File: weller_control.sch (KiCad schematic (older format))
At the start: 19 parts, among them J2 AudioJack3_Ground_SwitchTR, Q1 DMP2018LFK, U2 LTC4440ES6, U3 MCP603-xCH

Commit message: duży update, gotowe pcb
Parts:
- C11: footprint (none) -> Capacitor_SMD:C_0603_1608Metric
- R7: footprint Resistor_SMD:R_0402_1005Metric -> Resistor_SMD:R_0603_1608Metric
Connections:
- wire segments 51 -> 53
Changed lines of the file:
@@
 EESchema Schematic File Version 4
+LIBS:WELLER-cache
 EELAYER 29 0
 EELAYER END
@@
 F 0 "R7" V 3793 3050 50  0000 C CNN
 F 1 "100" V 3884 3050 50  0000 C CNN
-F 2 "Resistor_SMD:R_0402_1005Metric" V 3930 3050 50  0001 C CNN
+F 2 "Resistor_SMD:R_0603_1608Metric" V 3930 3050 50  0001 C CNN
 F 3 "~" H 4000 3050 50  0001 C CNN
 	1    4000 3050
@@
 Connection ~ 5750 6000
 Wire Wire Line
-	5750 6000 5750 6250
+	5750 6000 5750 6150
 Wire Wire Line
 	5750 5700 5750 6000
@@
 	1    0    0    -1
 $EndComp
-NoConn ~ 5750 5000
 Text Notes 7200 4700 0    50   ~ 0
 sprawdzenie czy na przypisanie pinów na footptincie piny się zgadza\n
@@
 F 0 "C11" H 6665 5496 50  0000 L CNN
 F 1 "n.c." H 6665 5405 50  0000 L CNN
-F 2 "" H 6588 5300 50  0001 C CNN
+F 2 "Capacitor_SMD:C_0603_1608Metric" H 6588 5300 50  0001 C CNN
 F 3 "~" H 6550 5450 50  0001 C CNN
 	1    6550 5450
@@
 Wire Wire Line
 	6600 2600 6650 2600
+Text HLabel 5750 4950 1    50   Input ~ 0
+3.3V_analog
+Wire Wire Line
+	5750 4950 5750 5000
+NoConn ~ 7150 3600
+$Comp
+L power:PWR_FLAG #FLG0104
+U 1 1 5CF26DBB
+P 5750 6150
+F 0 "#FLG0104" H 5750 6225 50  0001 C CNN
+F 1 "PWR_FLAG" V 5750 6278 50  0000 L CNN
+F 2 "" H 5750 6150 50  0001 C CNN
+F 3 "~" H 5750 6150 50  0001 C CNN
+	1    5750 6150
+	0    1    1    0
+$EndComp
+Connection ~ 5750 6150
+Wire Wire Line
+	5750 6150 5750 6250
 $EndSCHEMATC

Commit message: poprawki na sch
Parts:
- removed J2: AudioJack3_Ground_SwitchTR, Connector_Audio:Jack_3.5mm_CUI_SJ-3524-SMT_Horizontal, symbol Connector:AudioJack3_SwitchTR
- added J2: AudioJack2_Ground_SwitchT, Connector_Audio:Jack_3.5mm_CUI_SJ-3524-SMT_Horizontal, symbol Connector:AudioJack2_Ground_SwitchT
- U3: footprint Package_TO_SOT_SMD:SOT-23-5_HandSoldering -> TO_SOT_Packages_SMD:SOT-23-6
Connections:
- wire segments 53 -> 52
- no-connect marks 1 -> 0
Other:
- note added: "from tip: ground, sensor, heater"
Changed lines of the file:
@@
 EESchema Schematic File Version 4
 LIBS:WELLER-cache
-EELAYER 29 0
+EELAYER 26 0
 EELAYER END
 $Descr A4 11693 8268
@@
 L power:GND #PWR?
 U 1 1 5CBA0B9E
-P 7050 3950
+P 7350 3950
 AR Path="/5CB5C0EA/5CBA0B9E" Ref="#PWR?"  Part="1"
 AR Path="/5CB9B8FA/5CBA0B9E" Ref="#PWR0115"  Part="1"
-F 0 "#PWR0115" H 7050 3700 50  0001 C CNN
-F 1 "GND" H 7055 3777 50  0000 C CNN
-F 2 "" H 7050 3950 50  0001 C CNN
-F 3 "" H 7050 3950 50  0001 C CNN
-	1    7050 3950
-	1    0    0    -1
-$EndComp
-Wire Wire Line
-	7150 3800 7050 3800
-Wire Wire Line
-	7050 3800 7050 3950
-Wire Wire Line
-	7150 3700 7000 3700
-Text Label 7000 3700 2    50   ~ 0
-termocouple+
-Text Label 7050 3500 2    50   ~ 0
+F 0 "#PWR0115" H 7350 3700 50  0001 C CNN
+F 1 "GND" H 7355 3777 50  0000 C CNN
+F 2 "" H 7350 3950 50  0001 C CNN
+F 3 "" H 7350 3950 50  0001 C CNN
+	1    7350 3950
+	1    0    0    -1
+$EndComp
+Text Label 7050 3600 2    50   ~ 0
 heater
 Text HLabel 6300 2550 1    50   Input ~ 0
@@
 F 0 "U3" H 6194 5346 50  0000 L CNN
 F 1 "MCP603-xCH" H 6194 5255 50  0000 L CNN
-F 2 "Package_TO_SOT_SMD:SOT-23-5_HandSoldering" H 5850 5300 50  0001 L CNN
+F 2 "TO_SOT_Packages_SMD:SOT-23-6" H 5850 5300 50  0001 L CNN
 F 3 "https://www.tme.eu/Document/718e1e465ad4ed1ffbd9a510b0eda58e/mcp6031.pdf" H 5900 5500 50  0001 C CNN
 	1    5850 5300
 	1    0    0    -1
 $EndComp
-Text Notes 7200 4700 0    50   ~ 0
+Text Notes 7250 3150 0    50   ~ 0
 sprawdzenie czy na przypisanie pinów na footptincie piny się zgadza\n
 Text Label 4000 5200 2    50   ~ 0
@@
 Wire Wire Line
 	7250 5300 7050 5300
-Wire Wire Line
-	6900 3400 7150 3400
-Text HLabel 6900 3400 1    50   BiDi ~ 0
+Text HLabel 7000 3700 0    50   BiDi ~ 0
 weller_connected_pin
 Wire Wire Line
@@
 Wire Wire Line
 	5300 3500 6300 3500
-$Comp
-L Connector:AudioJack3_SwitchTR J2
-U 1 1 5CBFD79A
-P 7350 3700
-F 0 "J2" H 7070 3476 50  0000 R CNN
-F 1 "AudioJack3_Ground_SwitchTR" H 7070 3567 50  0000 R CNN
-F 2 "Connector_Audio:Jack_3.5mm_CUI_SJ-3524-SMT_Horizontal" H 7350 3700 50  0001 C CNN
-F 3 "~" H 7350 3700 50  0001 C CNN
-	1    7350 3700
-	-1   0    0    1
-$EndComp
 $Comp
 L Device:C C19
@@
 Wire Wire Line
 	5750 4950 5750 5000
-NoConn ~ 7150 3600
 $Comp
 L power:PWR_FLAG #FLG0104
@@
 Wire Wire Line
 	5750 6150 5750 6250
+$Comp
+L Connector:AudioJack2_Ground_SwitchT J2
+U 1 1 5CEFB0EB
+P 7350 3600
+F 0 "J2" H 7170 3570 50  0000 R CNN
+F 1 "AudioJack2_Ground_SwitchT" H 7170 3479 50  0000 R CNN
+F 2 "Connector_Audio:Jack_3.5mm_CUI_SJ-3524-SMT_Horizontal" H 7350 3600 50  0001 C CNN
+F 3 "~" H 7350 3600 50  0001 C CNN
+	1    7350 3600
+	-1   0    0    -1
+$EndComp
+Text Label 7100 3500 2    50   ~ 0
+termocouple+
+Wire Wire Line
+	7350 3900 7350 3950
+Wire Wire Line
+	7150 3700 7000 3700
+Wire Wire Line
+	7050 3600 7150 3600
+Text Notes 7250 3300 0    50   ~ 0
+from tip: ground, sensor, heater
 $EndSCHEMATC

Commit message: duży update, drc przechodzi
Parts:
- removed J2: AudioJack2_Ground_SwitchT, Connector_Audio:Jack_3.5mm_CUI_SJ-3524-SMT_Horizontal, symbol Connector:AudioJack2_Ground_SwitchT
- added J2: AudioJack3_Ground_SwitchR, symbols:Jack Audio 1503 20, symbol Connector:AudioJack3_Ground_SwitchR
- R7: footprint Resistor_SMD:R_0603_1608Metric -> Resistor_SMD:R_1206_3216Metric
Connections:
- wire segments 52 -> 54
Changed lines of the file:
@@
 EESchema Schematic File Version 4
 LIBS:WELLER-cache
-EELAYER 26 0
+EELAYER 29 0
 EELAYER END
 $Descr A4 11693 8268
@@
 Comment4 ""
 $EndDescr
-$Comp
-L power:GND #PWR?
-U 1 1 5CBA0B9E
-P 7350 3950
-AR Path="/5CB5C0EA/5CBA0B9E" Ref="#PWR?"  Part="1"
-AR Path="/5CB9B8FA/5CBA0B9E" Ref="#PWR0115"  Part="1"
-F 0 "#PWR0115" H 7350 3700 50  0001 C CNN
-F 1 "GND" H 7355 3777 50  0000 C CNN
-F 2 "" H 7350 3950 50  0001 C CNN
-F 3 "" H 7350 3950 50  0001 C CNN
-	1    7350 3950
-	1    0    0    -1
-$EndComp
-Text Label 7050 3600 2    50   ~ 0
-heater
 Text HLabel 6300 2550 1    50   Input ~ 0
 12V
@@
 F 0 "R7" V 3793 3050 50  0000 C CNN
 F 1 "100" V 3884 3050 50  0000 C CNN
-F 2 "Resistor_SMD:R_0603_1608Metric" V 3930 3050 50  0001 C CNN
+F 2 "Resistor_SMD:R_1206_3216Metric" V 3930 3050 50  0001 C CNN
 F 3 "~" H 4000 3050 50  0001 C CNN
 	1    4000 3050
@@
 	5200 2850 5100 2850
 Connection ~ 5100 2850
-Connection ~ 6300 3500
-Wire Wire Line
-	6300 3500 7150 3500
 Text HLabel 3550 3050 0    50   Input ~ 0
 HeaterDrivePWM
-$Comp
-L Transistor_FET:DMP3013SFV Q1
-U 1 1 5CBB49B6
-P 6200 3050
-F 0 "Q1" H 6406 3096 50  0000 L CNN
-F 1 "DMP2018LFK" H 6406 3005 50  0000 L CNN
-F 2 "Package_SON:Diodes_PowerDI3333-8" H 6400 2975 50  0001 L CIN
-F 3 "https://www.diodes.com/assets/Datasheets/DMP3013SFV.pdf" V 6200 3050 50  0001 L CNN
-	1    6200 3050
-	1    0    0    -1
-$EndComp
 Wire Wire Line
 	5100 3050 6000 3050
@@
 Connection ~ 5750 6000
 Wire Wire Line
-	5750 6000 5750 6150
-Wire Wire Line
 	5750 5700 5750 6000
 Wire Wire Line
@@
 	1    0    0    -1
 $EndComp
-Text Notes 7250 3150 0    50   ~ 0
+Text Notes 7100 2800 0    50   ~ 0
 sprawdzenie czy na przypisanie pinów na footptincie piny się zgadza\n
 Text Label 4000 5200 2    50   ~ 0
@@
 Wire Wire Line
 	7250 5300 7050 5300
-Text HLabel 7000 3700 0    50   BiDi ~ 0
+Text HLabel 7450 3400 0    50   BiDi ~ 0
 weller_connected_pin
 Wire Wire Line
@@
 Wire Wire Line
 	5750 4950 5750 5000
-$Comp
-L power:PWR_FLAG #FLG0104
-U 1 1 5CF26DBB
-P 5750 6150
-F 0 "#FLG0104" H 5750 6225 50  0001 C CNN
-F 1 "PWR_FLAG" V 5750 6278 50  0000 L CNN
-F 2 "" H 5750 6150 50  0001 C CNN
-F 3 "~" H 5750 6150 50  0001 C CNN
-	1    5750 6150
-	0    1    1    0
-$EndComp
-Connection ~ 5750 6150
-Wire Wire Line
-	5750 6150 5750 6250
-$Comp
-L Connector:AudioJack2_Ground_SwitchT J2
-U 1 1 5CEFB0EB
-P 7350 3600
-F 0 "J2" H 7170 3570 50  0000 R CNN
-F 1 "AudioJack2_Ground_SwitchT" H 7170 3479 50  0000 R CNN
-F 2 "Connector_Audio:Jack_3.5mm_CUI_SJ-3524-SMT_Horizontal" H 7350 3600 50  0001 C CNN
-F 3 "~" H 7350 3600 50  0001 C CNN
-	1    7350 3600
+Text Label 7550 3200 2    50   ~ 0
+termocouple+
+Wire Wire Line
+	7600 3400 7450 3400
+Text Notes 7100 2950 0    50   ~ 0
+from tip: ground, sensor, heater
+$Comp
+L Transistor_FET:DMP3013SFV Q1
+U 1 1 5CBB49B6
+P 6200 3050
+F 0 "Q1" H 6406 3096 50  0000 L CNN
+F 1 "DMP2018LFK" H 6406 3005 50  0000 L CNN
+F 2 "Package_SON:Diodes_PowerDI3333-8" H 6400 2975 50  0001 L CIN
+F 3 "https://www.diodes.com/assets/Datasheets/DMP3013SFV.pdf" V 6200 3050 50  0001 L CNN
+	1    6200 3050
+	1    0    0    -1
+$EndComp
+$Comp
+L power:GND #PWR?
+U 1 1 5CBA0B9E
+P 7800 3850
+AR Path="/5CB5C0EA/5CBA0B9E" Ref="#PWR?"  Part="1"
+AR Path="/5CB9B8FA/5CBA0B9E" Ref="#PWR0115"  Part="1"
+F 0 "#PWR0115" H 7800 3600 50  0001 C CNN
+F 1 "GND" H 7805 3677 50  0000 C CNN
+F 2 "" H 7800 3850 50  0001 C CNN
+F 3 "" H 7800 3850 50  0001 C CNN
+	1    7800 3850
+	1    0    0    -1
+$EndComp
+Wire Wire Line
+	7800 3800 7800 3850
+$Comp
+L Connector:AudioJack3_Ground_SwitchR J2
+U 1 1 5CFC3271
+P 7800 3300
+F 0 "J2" H 7520 3168 50  0000 R CNN
+F 1 "AudioJack3_Ground_SwitchR" H 7520 3077 50  0000 R CNN
+F 2 "symbols:Jack Audio 1503 20" H 7800 3300 50  0001 C CNN
+F 3 "~" H 7800 3300 50  0001 C CNN
+	1    7800 3300
 	-1   0    0    -1
 $EndComp
 Text Label 7100 3500 2    50   ~ 0
-termocouple+
-Wire Wire Line
-	7350 3900 7350 3950
-Wire Wire Line
-	7150 3700 7000 3700
-Wire Wire Line
-	7050 3600 7150 3600
-Text Notes 7250 3300 0    50   ~ 0
-from tip: ground, sensor, heater
+heater
+Wire Wire Line
+	7550 3200 7600 3200
+Wire Wire Line
+	6300 3500 7200 3500
+Connection ~ 6300 3500
+Wire Wire Line
+	7600 3300 7200 3300
+Wire Wire Line
+	7200 3300 7200 3500
+Connection ~ 7200 3500
+Wire Wire Line
+	7200 3500 7600 3500
+Wire Wire Line
+	5750 6000 5750 6250
 $EndSCHEMATC

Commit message: poprawki głownie na pcb zaokrąglenie strony z grotem
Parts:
- removed D6: 1n4148, Diode_SMD:D_0805_2012Metric, symbol Device:D
- removed U2: LTC4440ES6, Package_TO_SOT_SMD:SOT-23-6, symbol Driver_FET:LTC4440ES6
- added C26: 100n, Capacitor_SMD:C_0603_1608Metric_Pad1.05x0.95mm_HandSolder, symbol Device:C
- added D6: 1N4148, Diode_SMD:D_0805_2012Metric, symbol Diode:1N4148
- added U2: LTC4440IS6, Package_TO_SOT_SMD:SOT-23-6, symbol Driver_FET:LTC4440IS6
- C8: value 100n -> 10uF; footprint Capacitor_SMD:C_0603_1608Metric_Pad1.05x0.95mm_HandSolder -> Capacitor_SMD:C_0805_2012Metric
- Q1: Pole4 (none) -> ${KISYS3DMOD}/Package_DFN_QFN.3dshapes/DFN-8-1EP_3x3mm_P0.6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
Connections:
- wire segments 54 -> 57
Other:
- moved on the sheet: C8, R7
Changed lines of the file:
@@
 	6300 2550 6300 2600
 Wire Wire Line
-	6300 3250 6300 3500
-$Comp
-L Driver_FET:LTC4440ES6 U2
-U 1 1 5CBAC998
-P 4700 3050
-F 0 "U2" H 4700 3631 50  0000 C CNN
-F 1 "LTC4440ES6" H 4700 3540 50  0000 C CNN
-F 2 "Package_TO_SOT_SMD:SOT-23-6" H 4700 2650 50  0001 C CNN
-F 3 "https://www.analog.com/media/en/technical-documentation/data-sheets/4440fb.pdf" H 4600 3500 50  0001 C CNN
-	1    4700 3050
-	1    0    0    -1
-$EndComp
-Text HLabel 4600 2200 1    50   Input ~ 0
+	6300 3250 6300 3300
+Text HLabel 4550 2150 1    50   Input ~ 0
 12V
 Wire Wire Line
-	4600 2200 4600 2400
+	4550 2150 4550 2350
 $Comp
 L power:GND #PWR?
 U 1 1 5CBAEA63
-P 4700 3850
+P 4650 3650
 AR Path="/5CB5C0EA/5CBAEA63" Ref="#PWR?"  Part="1"
 AR Path="/5CB9B8FA/5CBAEA63" Ref="#PWR0116"  Part="1"
-F 0 "#PWR0116" H 4700 3600 50  0001 C CNN
-F 1 "GND" H 4705 3677 50  0000 C CNN
-F 2 "" H 4700 3850 50  0001 C CNN
-F 3 "" H 4700 3850 50  0001 C CNN
-	1    4700 3850
-	1    0    0    -1
-$EndComp
-Wire Wire Line
-	4700 3850 4700 3350
+F 0 "#PWR0116" H 4650 3400 50  0001 C CNN
+F 1 "GND" H 4655 3477 50  0000 C CNN
+F 2 "" H 4650 3650 50  0001 C CNN
+F 3 "" H 4650 3650 50  0001 C CNN
+	1    4650 3650
+	1    0    0    -1
+$EndComp
+Wire Wire Line
+	4650 3650 4650 3350
 $Comp
 L Device:R R7
 U 1 1 5CBB027F
-P 4000 3050
-F 0 "R7" V 3793 3050 50  0000 C CNN
-F 1 "100" V 3884 3050 50  0000 C CNN
-F 2 "Resistor_SMD:R_1206_3216Metric" V 3930 3050 50  0001 C CNN
-F 3 "~" H 4000 3050 50  0001 C CNN
-	1    4000 3050
+P 3800 3050
+F 0 "R7" V 3593 3050 50  0000 C CNN
+F 1 "100" V 3684 3050 50  0000 C CNN
+F 2 "Resistor_SMD:R_1206_3216Metric" V 3730 3050 50  0001 C CNN
+F 3 "~" H 3800 3050 50  0001 C CNN
+	1    3800 3050
 	0    1    1    0
 $EndComp
 Wire Wire Line
-	5100 3150 5200 3150
-Wire Wire Line
-	5300 3150 5300 3500
-$Comp
-L Device:D D6
-U 1 1 5CBB1370
-P 4900 2400
-F 0 "D6" H 4900 2184 50  0000 C CNN
-F 1 "1n4148" H 4900 2275 50  0000 C CNN
-F 2 "Diode_SMD:D_0805_2012Metric" H 4900 2400 50  0001 C CNN
-F 3 "~" H 4900 2400 50  0001 C CNN
-	1    4900 2400
-	-1   0    0    1
-$EndComp
-Wire Wire Line
-	4750 2400 4600 2400
-Connection ~ 4600 2400
-Wire Wire Line
-	4600 2400 4600 2650
-Wire Wire Line
-	5050 2400 5100 2400
-Wire Wire Line
-	5100 2400 5100 2850
-$Comp
-L Device:C C7
-U 1 1 5CBB2260
-P 5200 3000
-F 0 "C7" H 5315 3046 50  0000 L CNN
-F 1 "100n" H 5315 2955 50  0000 L CNN
-F 2 "Capacitor_SMD:C_0603_1608Metric_Pad1.05x0.95mm_HandSolder" H 5238 2850 50  0001 C CNN
-F 3 "~" H 5200 3000 50  0001 C CNN
-	1    5200 3000
-	1    0    0    -1
-$EndComp
-Connection ~ 5200 3150
-Wire Wire Line
-	5200 3150 5300 3150
-Wire Wire Line
-	5200 2850 5100 2850
-Connection ~ 5100 2850
-Text HLabel 3550 3050 0    50   Input ~ 0
+	4700 2350 4550 2350
+Connection ~ 4550 2350
+Text HLabel 3350 3050 0    50   Input ~ 0
 HeaterDrivePWM
 Wire Wire Line
-	5100 3050 6000 3050
-Wire Wire Line
-	3550 3050 3850 3050
-Wire Wire Line
-	4150 3050 4300 3050
+	3350 3050 3650 3050
 $Comp
 L Device:R R12
@@
 Text HLabel 7450 3400 0    50   BiDi ~ 0
 weller_connected_pin
-Wire Wire Line
-	5300 3850 5300 3800
-$Comp
-L power:GND #PWR?
-U 1 1 5CBA9A21
-P 5300 3850
-AR Path="/5CB5C0EA/5CBA9A21" Ref="#PWR?"  Part="1"
-AR Path="/5CB9B8FA/5CBA9A21" Ref="#PWR0122"  Part="1"
-F 0 "#PWR0122" H 5300 3600 50  0001 C CNN
-F 1 "GND" H 5305 3677 50  0000 C CNN
-F 2 "" H 5300 3850 50  0001 C CNN
-F 3 "" H 5300 3850 50  0001 C CNN
-	1    5300 3850
-	1    0    0    -1
-$EndComp
 $Comp
 L Device:C C8
 U 1 1 5CBA90B4
-P 5300 3650
-F 0 "C8" H 5415 3696 50  0000 L CNN
-F 1 "100n" H 5415 3605 50  0000 L CNN
-F 2 "Capacitor_SMD:C_0603_1608Metric_Pad1.05x0.95mm_HandSolder" H 5338 3500 50  0001 C CNN
-F 3 "~" H 5300 3650 50  0001 C CNN
-	1    5300 3650
-	1    0    0    -1
-$EndComp
-Connection ~ 5300 3500
-Wire Wire Line
-	5300 3500 6300 3500
+P 4850 2350
+F 0 "C8" H 4965 2396 50  0000 L CNN
+F 1 "10uF" H 4965 2305 50  0000 L CNN
+F 2 "Capacitor_SMD:C_0805_2012Metric" H 4888 2200 50  0001 C CNN
+F 3 "~" H 4850 2350 50  0001 C CNN
+	1    4850 2350
+	0    1    -1   0
+$EndComp
 $Comp
 L Device:C C19
@@
 F 2 "Package_SON:Diodes_PowerDI3333-8" H 6400 2975 50  0001 L CIN
 F 3 "https://www.diodes.com/assets/Datasheets/DMP3013SFV.pdf" V 6200 3050 50  0001 L CNN
+F 4 "${KISYS3DMOD}/Package_DFN_QFN.3dshapes/DFN-8-1EP_3x3mm_P0.65mm_EP1.55x2.4mm.wrl" H 6200 3050 50  0001 C CNN "Pole4"
 	1    6200 3050
-	1    0    0    -1
+	1    0    0    1
 $EndComp
 $Comp
@@
 Wire Wire Line
 	6300 3500 7200 3500
-Connection ~ 6300 3500
 Wire Wire Line
 	7600 3300 7200 3300
@@
 Wire Wire Line
 	5750 6000 5750 6250
+$Comp
+L Device:C C7
+U 1 1 5D187BE9
+P 4400 2350
+F 0 "C7" H 4515 2396 50  0000 L CNN
+F 1 "100n" H 4515 2305 50  0000 L CNN
+F 2 "Capacitor_SMD:C_0603_1608Metric_Pad1.05x0.95mm_HandSolder" H 4438 2200 50  0001 C CNN
+F 3 "~" H 4400 2350 50  0001 C CNN
+	1    4400 2350
+	0    1    -1   0
+$EndComp
+$Comp
+L power:GND #PWR?
+U 1 1 5D18AED0
+P 4150 2350
+AR Path="/5CB5C0EA/5D18AED0" Ref="#PWR?"  Part="1"
+AR Path="/5CB9B8FA/5D18AED0" Ref="#PWR0122"  Part="1"
+F 0 "#PWR0122" H 4150 2100 50  0001 C CNN
+F 1 "GND" H 4155 2177 50  0000 C CNN
+F 2 "" H 4150 2350 50  0001 C CNN
+F 3 "" H 4150 2350 50  0001 C CNN
+	1    4150 2350
+	0    1    1    0
+$EndComp
+Wire Wire Line
+	4150 2350 4250 2350
+$Comp
+L Driver_FET:LTC4440IS6 U2
+U 1 1 5D1044C6
+P 4650 3050
+F 0 "U2" H 4100 3550 50  0000 C CNN
+F 1 "LTC4440IS6" H 4250 3450 50  0000 C CNN
+F 2 "Package_TO_SOT_SMD:SOT-23-6" H 4650 2650 50  0001 C CNN
+F 3 "https://www.analog.com/media/en/technical-documentation/data-sheets/4440fb.pdf" H 4550 3500 50  0001 C CNN
+	1    4650 3050
+	1    0    0    -1
+$EndComp
+$Comp
+L Diode:1N4148 D6
+U 1 1 5D104CD3
+P 4950 2650
+F 0 "D6" H 4950 2434 50  0000 C CNN
+F 1 "1N4148" H 4950 2525 50  0000 C CNN
+F 2 "Diode_SMD:D_0805_2012Metric" H 4950 2475 50  0001 C CNN
+F 3 "https://assets.nexperia.com/documents/data-sheet/1N4148_1N4448.pdf" H 4950 2650 50  0001 C CNN
+	1    4950 2650
+	-1   0    0    1
+$EndComp
+Wire Wire Line
+	3950 3050 4250 3050
+Wire Wire Line
+	4550 2350 4550 2650
+$Comp
+L power:GND #PWR?
+U 1 1 5D10E4EA
+P 5100 2350
+AR Path="/5CB5C0EA/5D10E4EA" Ref="#PWR?"  Part="1"
+AR Path="/5CB9B8FA/5D10E4EA" Ref="#PWR0143"  Part="1"
+F 0 "#PWR0143" H 5100 2100 50  0001 C CNN
+F 1 "GND" H 5105 2177 50  0000 C CNN
+F 2 "" H 5100 2350 50  0001 C CNN
+F 3 "" H 5100 2350 50  0001 C CNN
+	1    5100 2350
+	0    -1   -1   0
+$EndComp
+Wire Wire Line
+	5000 2350 5100 2350
+Wire Wire Line
+	5050 3150 5150 3150
+Wire Wire Line
+	5850 3150 5850 3300
+Wire Wire Line
+	5850 3300 6300 3300
+Connection ~ 6300 3300
+Wire Wire Line
+	6300 3300 6300 3500
+Wire Wire Line
+	5050 3050 6000 3050
+Wire Wire Line
+	4550 2650 4800 2650
+Connection ~ 4550 2650
+Wire Wire Line
+	5150 2650 5100 2650
+Wire Wire Line
+	5050 2850 5150 2850
+Wire Wire Line
+	5150 2850 5150 2650
+$Comp
+L Device:C C26
+U 1 1 5D1181DD
+P 5150 3000
+F 0 "C26" H 5265 3046 50  0000 L CNN
+F 1 "100n" H 5265 2955 50  0000 L CNN
+F 2 "Capacitor_SMD:C_0603_1608Metric_Pad1.05x0.95mm_HandSolder" H 5188 2850 50  0001 C CNN
+F 3 "~" H 5150 3000 50  0001 C CNN
+	1    5150 3000
+	1    0    0    1
+$EndComp
+Connection ~ 5150 3150
+Wire Wire Line
+	5150 3150 5850 3150
+Connection ~ 5150 2850
 $EndSCHEMATC

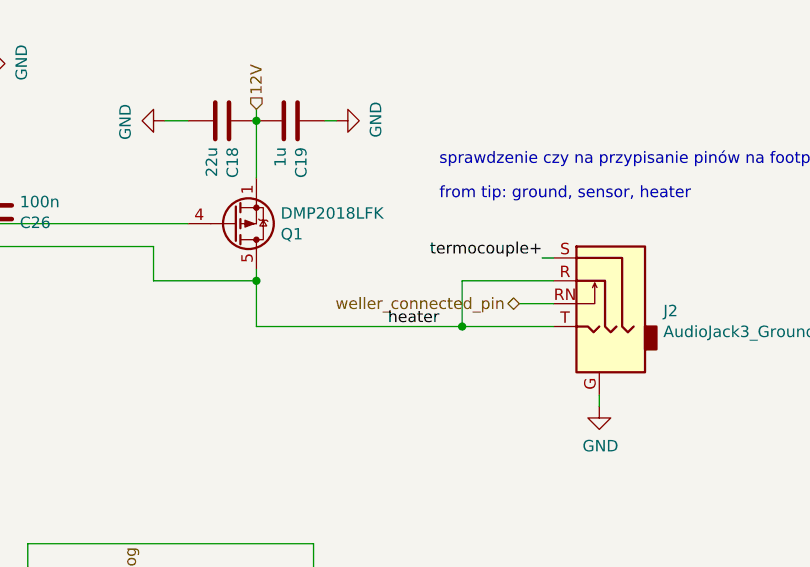
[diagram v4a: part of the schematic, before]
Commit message: wyciecie przy gnieździe jack - dodanie 3d gniazda, update jpg
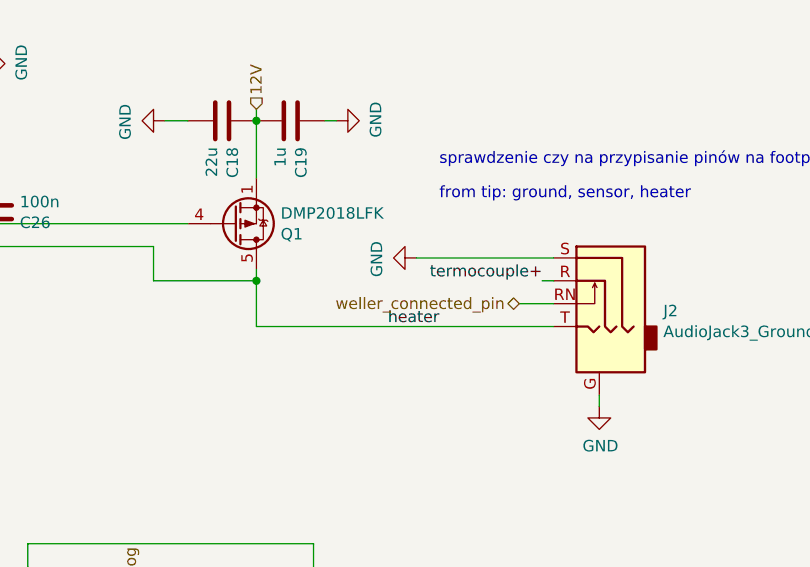
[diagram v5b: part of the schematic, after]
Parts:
- J2: footprint symbols:Jack Audio 1503 20 -> symbols:Jack Audio150320cutout
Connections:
- net GND: now also J2.S
- net heater: no longer J2.R
- net termocouple+: now also J2.R; no longer J2.S
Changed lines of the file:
@@
 Wire Wire Line
 	5750 4950 5750 5000
-Text Label 7550 3200 2    50   ~ 0
+Text Label 7550 3300 2    50   ~ 0
 termocouple+
 Wire Wire Line
@@
 F 0 "J2" H 7520 3168 50  0000 R CNN
 F 1 "AudioJack3_Ground_SwitchR" H 7520 3077 50  0000 R CNN
-F 2 "symbols:Jack Audio 1503 20" H 7800 3300 50  0001 C CNN
+F 2 "symbols:Jack Audio150320cutout" H 7800 3300 50  0001 C CNN
 F 3 "~" H 7800 3300 50  0001 C CNN
 	1    7800 3300
@@
 Text Label 7100 3500 2    50   ~ 0
 heater
-Wire Wire Line
-	7550 3200 7600 3200
-Wire Wire Line
-	6300 3500 7200 3500
-Wire Wire Line
-	7600 3300 7200 3300
-Wire Wire Line
-	7200 3300 7200 3500
-Connection ~ 7200 3500
-Wire Wire Line
-	7200 3500 7600 3500
 Wire Wire Line
 	5750 6000 5750 6250
@@
 	5150 3150 5850 3150
 Connection ~ 5150 2850
+Wire Wire Line
+	6300 3500 7600 3500
+Wire Wire Line
+	7550 3300 7600 3300
+$Comp
+L power:GND #PWR?
+U 1 1 5D11E72E
+P 7000 3200
+AR Path="/5CB5C0EA/5D11E72E" Ref="#PWR?"  Part="1"
+AR Path="/5CB9B8FA/5D11E72E" Ref="#PWR0148"  Part="1"
+F 0 "#PWR0148" H 7000 2950 50  0001 C CNN
+F 1 "GND" H 7005 3027 50  0000 C CNN
+F 2 "" H 7000 3200 50  0001 C CNN
+F 3 "" H 7000 3200 50  0001 C CNN
+	1    7000 3200
+	0    1    1    0
+$EndComp
+Wire Wire Line
+	7000 3200 7600 3200
 $EndSCHEMATC
